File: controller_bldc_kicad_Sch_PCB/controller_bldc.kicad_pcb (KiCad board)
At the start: 2 copper layers, 178.1 x 101.9 mm, 57 parts, among them J1 Battery Supply, J2 Emergency Button OUT, J3 Emergency Button IN, J4 Brake, J5 Throttle, J6 LM35, J7 Hall Sensors, J8 Nextion Nx3224T028, J9 BLDC Motor, K1 ADW11, Q1 IRF1010N, Q2 IRF1010N, Q3 IRF1010N, Q4 IRF1010N, Q5 IRF1010N, Q6 IRF1010N, SW1 ON_OFF, SW2 OPC, U1 ESP32-DEVKITC-32D, U2 LM317_TO-220, U3 LM7805_TO220, U4 IR2103, U8 IR2103, U9 IR2103

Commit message: This fixes PCB and Schematic, closes #5, closes #6, closes #7, closes #8
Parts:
- removed J2: Emergency Button OUT, Connector_Phoenix_GMSTB:PhoenixContact_GMSTBA_2,5_2-G_1x02_P7.50mm_Horizontal
- removed J3: Emergency Button IN, Connector_Phoenix_GMSTB:PhoenixContact_GMSTBA_2,5_2-G_1x02_P7.50mm_Horizontal
- added D4: 1N4728A, Diode_THT:D_DO-41_SOD81_P10.16mm_Horizontal, F.Cu at (167.7, 67.9)
- added D5: 1N4728A, Diode_THT:D_DO-41_SOD81_P10.16mm_Horizontal, F.Cu at (157.6, 62.4)
- added D6: 1N4148, Diode_THT:D_DO-35_SOD27_P7.62mm_Horizontal, F.Cu at (158.8, 86.3)
- added D7: 1N4148, Diode_THT:D_DO-35_SOD27_P7.62mm_Horizontal, F.Cu at (146.6, 79.6)
- added D8: 1N4148, Diode_THT:D_DO-35_SOD27_P7.62mm_Horizontal, F.Cu at (154.6, 74.6)
- added D9: 1N4004, Diode_THT:D_DO-35_SOD27_P7.62mm_Horizontal, F.Cu at (4.81, 27.4)
- added Q7: PN2222A, Package_TO_SOT_THT:TO-92_Inline, F.Cu at (21.3, 19.8)
- added R17: 5.2k, Resistor_THT:R_Axial_DIN0207_L6.3mm_D2.5mm_P10.16mm_Horizontal, F.Cu at (167.7, 56.9)
- added R18: 220, Resistor_THT:R_Axial_DIN0207_L6.3mm_D2.5mm_P10.16mm_Horizontal, F.Cu at (157.6, 81.2)
- added R19: 4.7k, Resistor_THT:R_Axial_DIN0207_L6.3mm_D2.5mm_P10.16mm_Horizontal, F.Cu at (125.0, 87.8)
- added R20: 15k, Resistor_THT:R_Axial_DIN0207_L6.3mm_D2.5mm_P10.16mm_Horizontal, F.Cu at (115.8, 91.4)
- added R21: 15k, Resistor_THT:R_Axial_DIN0207_L6.3mm_D2.5mm_P10.16mm_Horizontal, F.Cu at (92.5, 77.7)
- added R22: 15k, Resistor_THT:R_Axial_DIN0207_L6.3mm_D2.5mm_P10.16mm_Horizontal, F.Cu at (97.0, 77.7)
- added R23: 150k, Resistor_THT:R_Axial_DIN0207_L6.3mm_D2.5mm_P10.16mm_Horizontal, F.Cu at (118.9, 77.7)
- added R24: 150k, Resistor_THT:R_Axial_DIN0207_L6.3mm_D2.5mm_P10.16mm_Horizontal, F.Cu at (101.6, 77.7)
- added R25: 2k, Resistor_THT:R_Axial_DIN0207_L6.3mm_D2.5mm_P10.16mm_Horizontal, F.Cu at (12.1, 36.3)
- added R26: 2.5k, Resistor_THT:R_Axial_DIN0207_L6.3mm_D2.5mm_P10.16mm_Horizontal, F.Cu at (115.8, 69.0)
- added R27: 2.5k, Resistor_THT:R_Axial_DIN0207_L6.3mm_D2.5mm_P10.16mm_Horizontal, F.Cu at (105.7, 75.1)
- added R28: 1.2k, Resistor_THT:R_Axial_DIN0207_L6.3mm_D2.5mm_P10.16mm_Horizontal, F.Cu at (157.5, 47.7)
- added U5: LM2596SOURCE, Package_TO_SOT_THT_Electeam:LM2596DCSource_Electeam, F.Cu at (102.4, 106.7)
- C5: value 33uF -> 0.47uF; footprint Capacitor_THT:CP_Radial_D8.0mm_P3.50mm -> Capacitor_THT:C_Disc_D7.5mm_W5.0mm_P10.00mm
- C6: value 100uF -> 47uF; footprint Capacitor_THT:CP_Radial_D6.3mm_P2.50mm -> Capacitor_THT:CP_Radial_D8.0mm_P3.80mm
- K1: value ADW11 -> RAYEX-L90B; footprint Relay_THT:Relay_1P1T_NO_10x24x18.8mm_Panasonic_ADW11xxxxW_THT -> Relay_THT:Relay_SPST_RAYEX-L90B
- R12: value R -> 1.5k
- R16, R4: value 2.2k -> 10k
- U2: value LM317_TO-220 -> MC1458P; footprint Package_TO_SOT_THT_Electeam:TO-220-3_Horizontal_TabDown -> Package_DIP:DIP-8_W7.62mm_LongPads
- U3: value LM7805_TO220 -> LM2596SOURCE_Pin2; footprint Package_TO_SOT_THT_Electeam:TO-220-3_Horizontal_TabDown -> Package_TO_SOT_THT_Electeam:LM2596DCSourcePin2_Electeam
- moved C1 197.8 mm to (37.1, 13.7), turned to 270 degrees
- moved D3 193.5 mm to (89.0, 11.7), turned to 270 degrees
- moved U4 192.3 mm to (83.2, 11.7), turned to 270 degrees
- moved U8 192.0 mm to (46.1, 12.0), turned to 270 degrees
- moved D2 190.3 mm to (70.7, 12.0), turned to 270 degrees
- moved U9 190.1 mm to (64.4, 12.0), turned to 270 degrees
- moved D1 185.0 mm to (52.3, 11.6), turned to 270 degrees
- moved C4 178.2 mm to (84.4, 21.9), turned to 180 degrees
- moved C2 177.5 mm to (47.3, 22.2), turned to 180 degrees
- moved C3 175.7 mm to (65.6, 22.2), turned to 180 degrees
- moved R4 175.5 mm to (42.4, 26.1), turned to 270 degrees
- moved R1 175.4 mm to (19.7, 36.3), turned to 90 degrees
- moved R2 170.2 mm to (27.3, 36.3), turned to 90 degrees
- moved R3 165.9 mm to (34.9, 36.3), turned to 90 degrees
- moved R7 157.8 mm to (87.9, 36.3), turned to 90 degrees
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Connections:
- net Net-(C13-Pad2) renamed Current_Sensor_AO
- C1 pad 1: Voltage_Sensor -> GND
- C1 pad 2: Net-(C1-Pad2) -> Voltage_Sensor
- C13 pad 1: Current_Sensor_IN -> GND
- C5 pad 1: +12V -> Net-(C5-Pad1)
- C5 pad 2: GND -> Net-(C5-Pad2)
- C6 pad 1: +5V -> GND
- C6 pad 2: GND -> Net-(C6-Pad2)
- J6 pad 2: LM35 -> LM35-RAW
- R4 pad 1: Net-(C1-Pad2) -> Voltage_Sensor
- SW2 pad 1: +12V -> Net-(Q7-Pad2)
- SW2 pad 2: Net-(K1-Pad1) -> GND
- U1 pad 10: LM35 -> Brake
- U1 pad 11: Brake -> (no net)
- U1 pad 18: (no net) -> LM35
- U1 pad 19: (no net) -> Current_Sensor_IN
- U1 pad 20: (no net) -> Throttle
- U1 pad 26: Throttle -> (no net)
- U1 pad 27: Current_Sensor_IN -> (no net)
- U1 pad 30: +5V -> +12V
- U2 pad 1: GND -> Net-(R23-Pad2)
- U2 pad 2: +12V -> 1IN-
- U2 pad 3: +36V -> Net-(R19-Pad1)
- U3 pad 1: +36V -> +12V
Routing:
- net GND: track 405.6 -> 0.00 mm
- net +5V: track 211.6 -> 0.00 mm
- net 36V-Power: track 139.8 -> 0.00 mm
- net +36V: track 139.6 -> 0.00 mm, vias 1 -> 0
- net +12V: track 137.1 -> 0.00 mm
- net PH3: track 103.5 -> 0.00 mm
- net PH1: track 101.0 -> 0.00 mm
- net PH2: track 97.9 -> 0.00 mm
- net Throttle: track 74.6 -> 0.00 mm
- net LM35: track 65.7 -> 0.00 mm
- net RX-LCD: track 62.9 -> 0.00 mm
- net TX-LCD: track 57.4 -> 0.00 mm
- net Current_Sensor: track 55.8 -> 0.00 mm
- net HALL-A: track 53.7 -> 0.00 mm
- net HIN3: track 51.9 -> 0.00 mm
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- removed copper zone on B.Cu, net +36V
- removed copper zone on F.Cu, net 36V-Power
- removed copper zone on B.Cu, net Current_Sensor
- removed copper zone on B.Cu, net GND
- removed copper zone on F.Cu, net GND
- removed copper zone on B.Cu, net Net-(F1-Pad1)
- removed copper zone on B.Cu, net Net-(F1-Pad2)
- removed copper zone on B.Cu, net Net-(J2-Pad1)
- removed copper zone on B.Cu, net Net-(J3-Pad1)
- removed copper zone on B.Cu, net PH1
- removed copper zone on F.Cu, net PH1
- removed copper zone on B.Cu, net PH2
- removed copper zone on F.Cu, net PH2
- removed copper zone on B.Cu, net PH3
- removed copper zone on F.Cu, net PH3
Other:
- board size 178.1 x 101.9 mm -> 210 x 125 mm

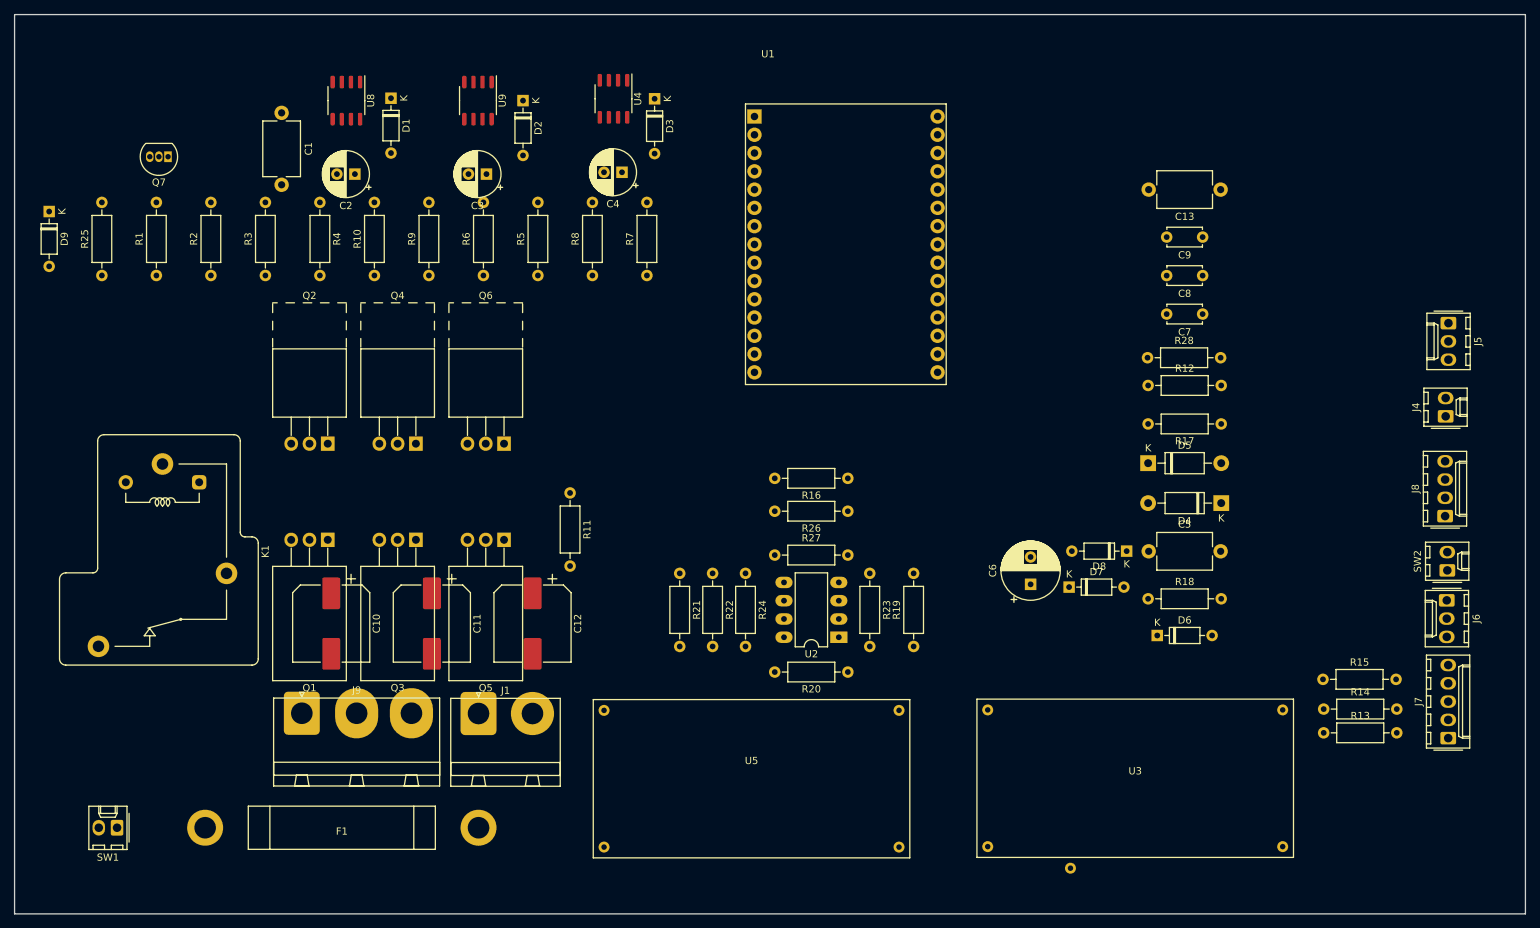
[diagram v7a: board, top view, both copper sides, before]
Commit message: PCB Finished, this is version 2.0. Closes #9 and closes #10.
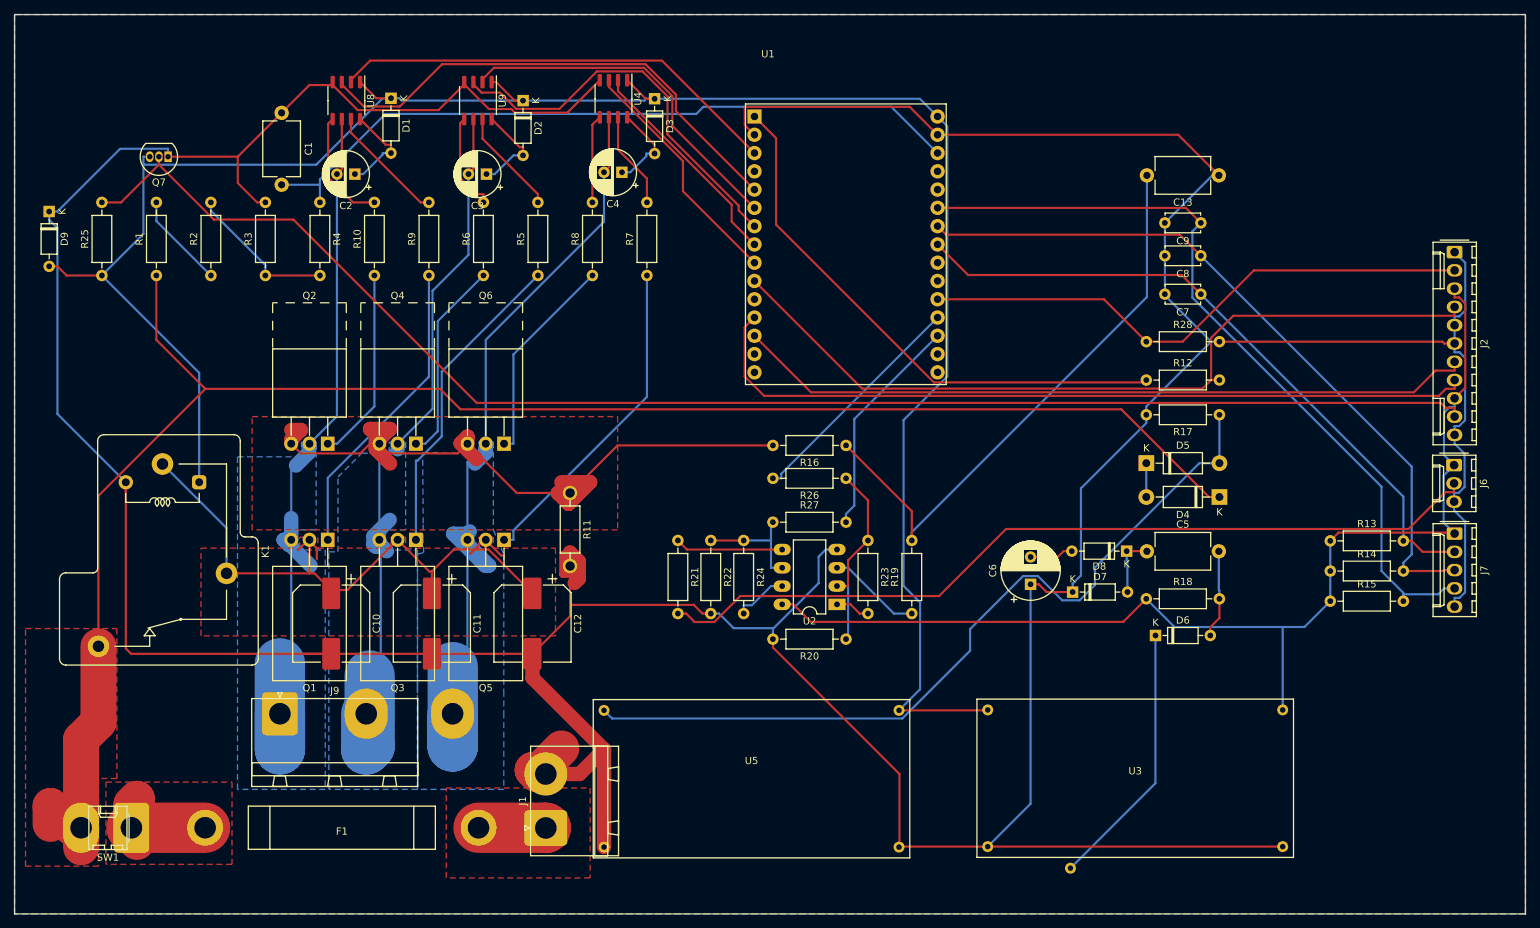
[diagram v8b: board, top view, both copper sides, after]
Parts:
- removed J4: Brake, Connector_Molex:Molex_KK-254_AE-6410-02A_1x02_P2.54mm_Vertical
- removed J5: Throttle, Connector_Molex:Molex_KK-254_AE-6410-03A_1x03_P2.54mm_Vertical
- removed J8: Nextion Nx3224T028, Connector_Molex:Molex_KK-254_AE-6410-04A_1x04_P2.54mm_Vertical
- removed SW2: OPC, Connector_Molex:Molex_KK-254_AE-6410-02A_1x02_P2.54mm_Vertical
- added J2: Conn_01x11_Male, Connector_Molex:Molex_KK-254_AE-6410-11A_1x11_P2.54mm_Vertical, F.Cu at (200.2, 33.0)
- C1: value 0.1uF -> 1uF
- moved J7 28.4 mm to (200.2, 72.1), turned to 270 degrees
- moved R13 26.7 mm to (182.9, 73.2)
- moved R14 19.2 mm to (182.9, 77.3)
- moved J6 18.8 mm to (200.1, 62.6)
- moved J1 18.5 mm to (73.8, 113.1), turned to 90 degrees
- moved R15 10.9 mm to (182.9, 81.5)
- moved R19 4.58 mm to (124.7, 83.3)
- moved R20 4.58 mm to (115.6, 86.8)
- moved R21 4.58 mm to (92.2, 73.1)
- moved R22 4.58 mm to (96.8, 73.1)
- moved R23 4.58 mm to (118.6, 73.1)
- moved R24 4.58 mm to (101.3, 73.1)
- moved R26 4.58 mm to (115.6, 64.5)
- moved R27 4.58 mm to (105.4, 70.6)
- moved U2 4.58 mm to (114.3, 82.0)
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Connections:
- net Net-(Q7-Pad2) renamed OPC_1
- D9 pad 1: Net-(D9-Pad1) -> GND
- K1 pad A2: Net-(D9-Pad1) -> GND
- Q7 pad 3: Net-(D9-Pad1) -> +12V
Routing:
- net GND: track 0.00 -> 727.3 mm
- net +12V: track 0.00 -> 293.1 mm
- net +36V: track 0.00 -> 244.7 mm
- net OPC_1: track 0.00 -> 206.5 mm
- net +5V: track 0.00 -> 157.8 mm
- net PH3: track 0.00 -> 125.9 mm
- net LM35-RAW: track 0.00 -> 117.1 mm
- net PH2: track 0.00 -> 116.2 mm
- net Brake: track 0.00 -> 113.5 mm
- net Net-(D5-Pad2): track 0.00 -> 113.4 mm
- net PH1: track 0.00 -> 113.1 mm
- net TX-LCD: track 0.00 -> 110.2 mm
- net HALL-C: track 0.00 -> 110.1 mm
- net Current_Sensor: track 0.00 -> 107.5 mm
- net RX-LCD: track 0.00 -> 103.0 mm
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- added copper zone on F.Cu, net +36V
- added copper zone on F.Cu, net 36V-Power
- added copper zone on F.Cu, net Current_Sensor
- added copper zone on B.Cu, net GND
- added copper zone on F.Cu, net GND
- added copper zone on F.Cu, net Net-(F1-Pad1)
- added copper zone on F.Cu, net Net-(F1-Pad2)
- added copper zone on B.Cu, net PH1
- added copper zone on B.Cu, net PH2
- added copper zone on B.Cu, net PH3
